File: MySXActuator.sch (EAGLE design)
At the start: 9 parts, among them Q1 2N7002, Q2 IRF530, X2 MKDSN1,5/5-5,08

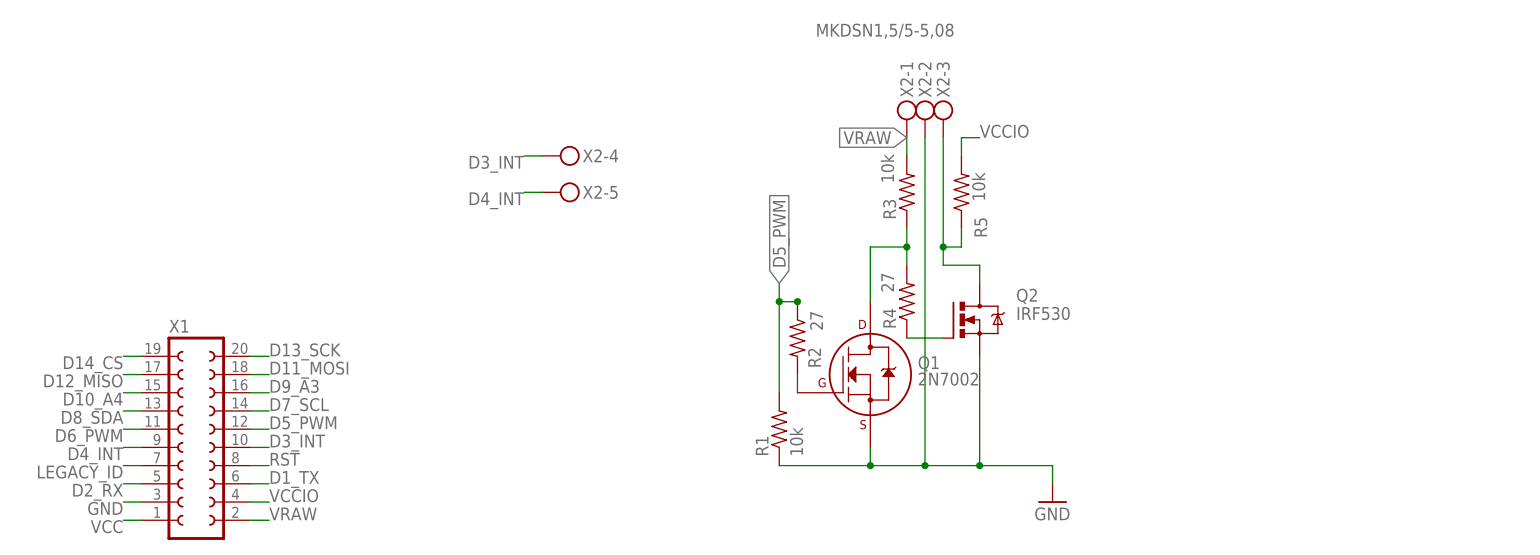
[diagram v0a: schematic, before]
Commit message: enlarge traces widths + add ldo
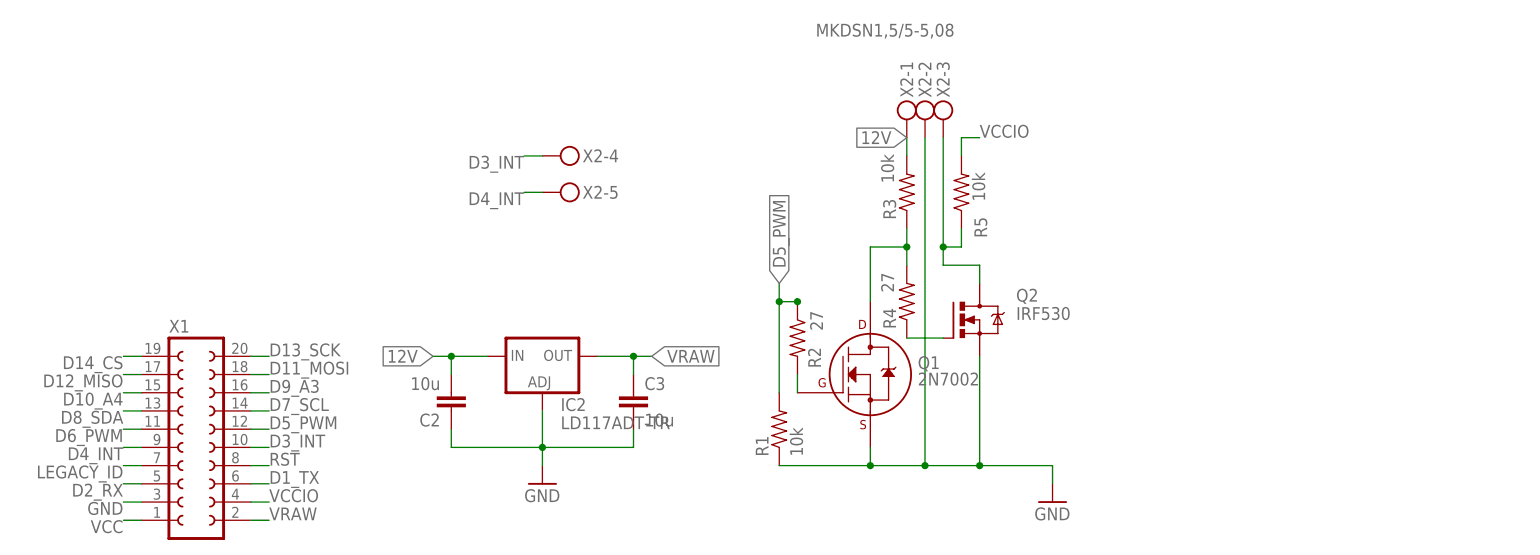
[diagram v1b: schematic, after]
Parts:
- added C2: 10u, SparkFun-Passives:CAP1206
- added C3: 10u, SparkFun-Passives:CAP0603-CAP
- added IC2: LD117ADT-TR, v-reg:LD117ADT-TR
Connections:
- new net 12V: C2.2, IC2.IN, R3.2, X2-1.KL
- net GND: now also C2.1, C3.2, IC2.ADJ
- net VRAW: now also C3.1, IC2.OUT; no longer R3.2, X2-1.KL
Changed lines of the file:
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@@
 </variantdefs>
 <classes>
-<class number="0" name="default" width="0.2032" drill="0.4064">
-<clearance class="0" value="0.2032"/>
+<class number="0" name="default" width="0.3048" drill="0.4064">
+<clearance class="0" value="0.2286"/>
 </class>
-<class number="1" name="Power" width="0.4064" drill="0.4064">
-<clearance class="1" value="0.2032"/>
+<class number="1" name="Power" width="0.6096" drill="0.4064">
+<clearance class="1" value="0.2286"/>
 </class>
 <class number="2" name="led power" width="1.524" drill="0.4064">
-<clearance class="2" value="0.2032"/>
+<clearance class="2" value="0.2286"/>
 </class>
 </classes>
@@
 <part name="R4" library="SparkFun-Passives" deviceset="RESISTOR" device="0603-RES" value="27"/>
 <part name="X2" library="con-phoenix-508" deviceset="MKDSN1,5/5-5,08" device=""/>
+<part name="C2" library="SparkFun-Passives" deviceset="CAP" device="1206" value="10u"/>
+<part name="C3" library="SparkFun-Passives" deviceset="CAP" device="0603-CAP" value="10u"/>
+<part name="GND5" library="supply1" deviceset="GND" device=""/>
+<part name="IC2" library="v-reg" deviceset="LD117A?*" device="DT" technology="-TR"/>
 </parts>
 <sheets>
@@
 <instance part="X2" gate="-4" x="60.96" y="99.06"/>
 <instance part="X2" gate="-5" x="60.96" y="93.98"/>
+<instance part="C2" gate="G$1" x="45.72" y="66.04" rot="R180"/>
+<instance part="C3" gate="G$1" x="71.12" y="63.5"/>
+<instance part="GND5" gate="1" x="58.42" y="53.34"/>
+<instance part="IC2" gate="G$1" x="58.42" y="71.12"/>
 </instances>
 <busses>
@@
 <pinref part="GND4" gate="1" pin="GND"/>
 <pinref part="R1" gate="G$1" pin="1"/>
-<pinref part="Q2" gate="G$1" pin="S"/>
-<wire x1="119.38" y1="71.12" x2="119.38" y2="55.88" width="0.1524" layer="91"/>
 <wire x1="111.76" y1="101.6" x2="111.76" y2="55.88" width="0.1524" layer="91"/>
 <pinref part="Q1" gate="G$1" pin="S"/>
@@
 <junction x="104.14" y="55.88"/>
 <junction x="111.76" y="55.88"/>
+<pinref part="X2" gate="-2" pin="KL"/>
+<pinref part="Q2" gate="G$1" pin="S"/>
+<wire x1="119.38" y1="71.12" x2="119.38" y2="55.88" width="0.1524" layer="91"/>
 <junction x="119.38" y="55.88"/>
-<pinref part="X2" gate="-2" pin="KL"/>
+</segment>
+<segment>
+<wire x1="58.42" y1="63.5" x2="58.42" y2="58.42" width="0.1524" layer="91"/>
+<pinref part="C3" gate="G$1" pin="2"/>
+<wire x1="71.12" y1="60.96" x2="71.12" y2="58.42" width="0.1524" layer="91"/>
+<wire x1="71.12" y1="58.42" x2="58.42" y2="58.42" width="0.1524" layer="91"/>
+<pinref part="C2" gate="G$1" pin="1"/>
+<wire x1="58.42" y1="58.42" x2="45.72" y2="58.42" width="0.1524" layer="91"/>
+<wire x1="45.72" y1="58.42" x2="45.72" y2="60.96" width="0.1524" layer="91"/>
+<wire x1="58.42" y1="58.42" x2="58.42" y2="55.88" width="0.1524" layer="91"/>
+<pinref part="GND5" gate="1" pin="GND"/>
+<junction x="58.42" y="58.42"/>
+<pinref part="IC2" gate="G$1" pin="ADJ"/>
 </segment>
 </net>
@@
 </segment>
 <segment>
-<pinref part="R3" gate="G$1" pin="2"/>
-<wire x1="109.22" y1="101.6" x2="109.22" y2="99.06" width="0.1524" layer="91"/>
-<pinref part="X2" gate="-1" pin="KL"/>
-<label x="109.22" y="101.6" size="1.778" layer="95" rot="R180" xref="yes"/>
+<pinref part="C3" gate="G$1" pin="1"/>
+<wire x1="71.12" y1="68.58" x2="71.12" y2="71.12" width="0.1524" layer="91"/>
+<wire x1="66.04" y1="71.12" x2="71.12" y2="71.12" width="0.1524" layer="91"/>
+<wire x1="71.12" y1="71.12" x2="73.66" y2="71.12" width="0.1524" layer="91"/>
+<label x="73.66" y="71.12" size="1.778" layer="95" xref="yes"/>
+<junction x="71.12" y="71.12"/>
+<pinref part="IC2" gate="G$1" pin="OUT"/>
 </segment>
 </net>
@@
 </segment>
 </net>
+<net name="12V" class="1">
+<segment>
+<pinref part="C2" gate="G$1" pin="2"/>
+<wire x1="45.72" y1="68.58" x2="45.72" y2="71.12" width="0.1524" layer="91"/>
+<wire x1="45.72" y1="71.12" x2="50.8" y2="71.12" width="0.1524" layer="91"/>
+<wire x1="45.72" y1="71.12" x2="43.18" y2="71.12" width="0.1524" layer="91"/>
+<label x="43.18" y="71.12" size="1.778" layer="95" rot="MR0" xref="yes"/>
+<junction x="45.72" y="71.12"/>
+<pinref part="IC2" gate="G$1" pin="IN"/>
+</segment>
+<segment>
+<pinref part="R3" gate="G$1" pin="2"/>
+<wire x1="109.22" y1="101.6" x2="109.22" y2="99.06" width="0.1524" layer="91"/>
+<pinref part="X2" gate="-1" pin="KL"/>
+<label x="109.22" y="101.6" size="1.778" layer="95" rot="R180" xref="yes"/>
+</segment>
+</net>

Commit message: add second dimmer
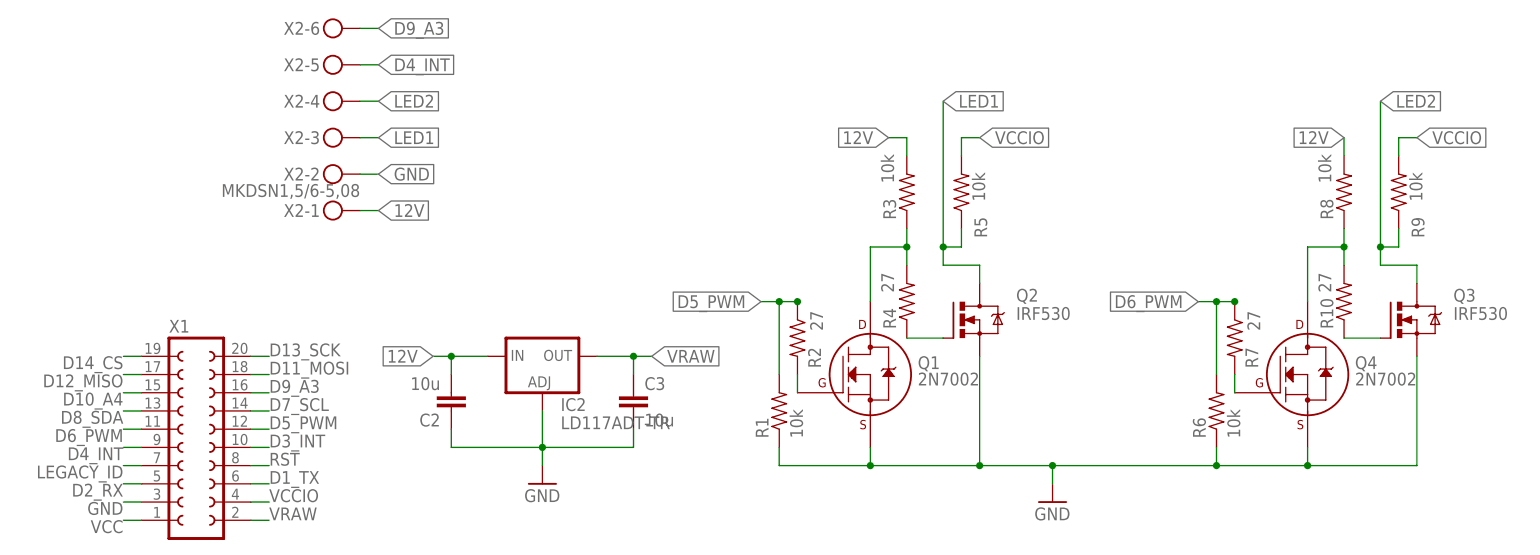
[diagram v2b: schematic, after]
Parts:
- added Q3: IRF530, transistor-power:IRF530
- added Q4: 2N7002, transistors:2N7002_SOT23
- added R10, R7: 27, SparkFun-Passives:RESISTOR0603-RES
- added R6, R8, R9: 10k, SparkFun-Passives:RESISTOR0603-RES
- X2: value MKDSN1,5/5-5,08 -> MKDSN1,5/6-5,08; device con-phoenix-508:MKDSN1,5/5-5,08 -> con-phoenix-508:MKDSN1,5/6-5,08
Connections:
- net N$10 renamed LED1
- new net LED2: Q3.D, R9.1, X2-4.KL
- new net N$2: Q4.G, R7.2
- new net N$3: Q4.D, R10.2, R8.1
- new net N$4: Q3.G, R10.1
- net 12V: now also R8.2
- net D3_INT: no longer X2-4.KL
- net D6_PWM: now also R6.2, R7.1
- net D9_A3: now also X2-6.KL
- net GND: now also Q3.S, Q4.S, R6.1
- net VCCIO: now also R9.2
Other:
- moved on the sheet: R1, X2-1, X2-2, X2-3, X2-4, X2-5
